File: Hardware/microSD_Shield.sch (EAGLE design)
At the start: 19 parts, among them J1 AVR_SPI_PRG_6NS, U1 USD-SOCKETNEW, U2 ARDUINO_R3_SHIELDNOLABELS, U3 HEX_CONVERTER

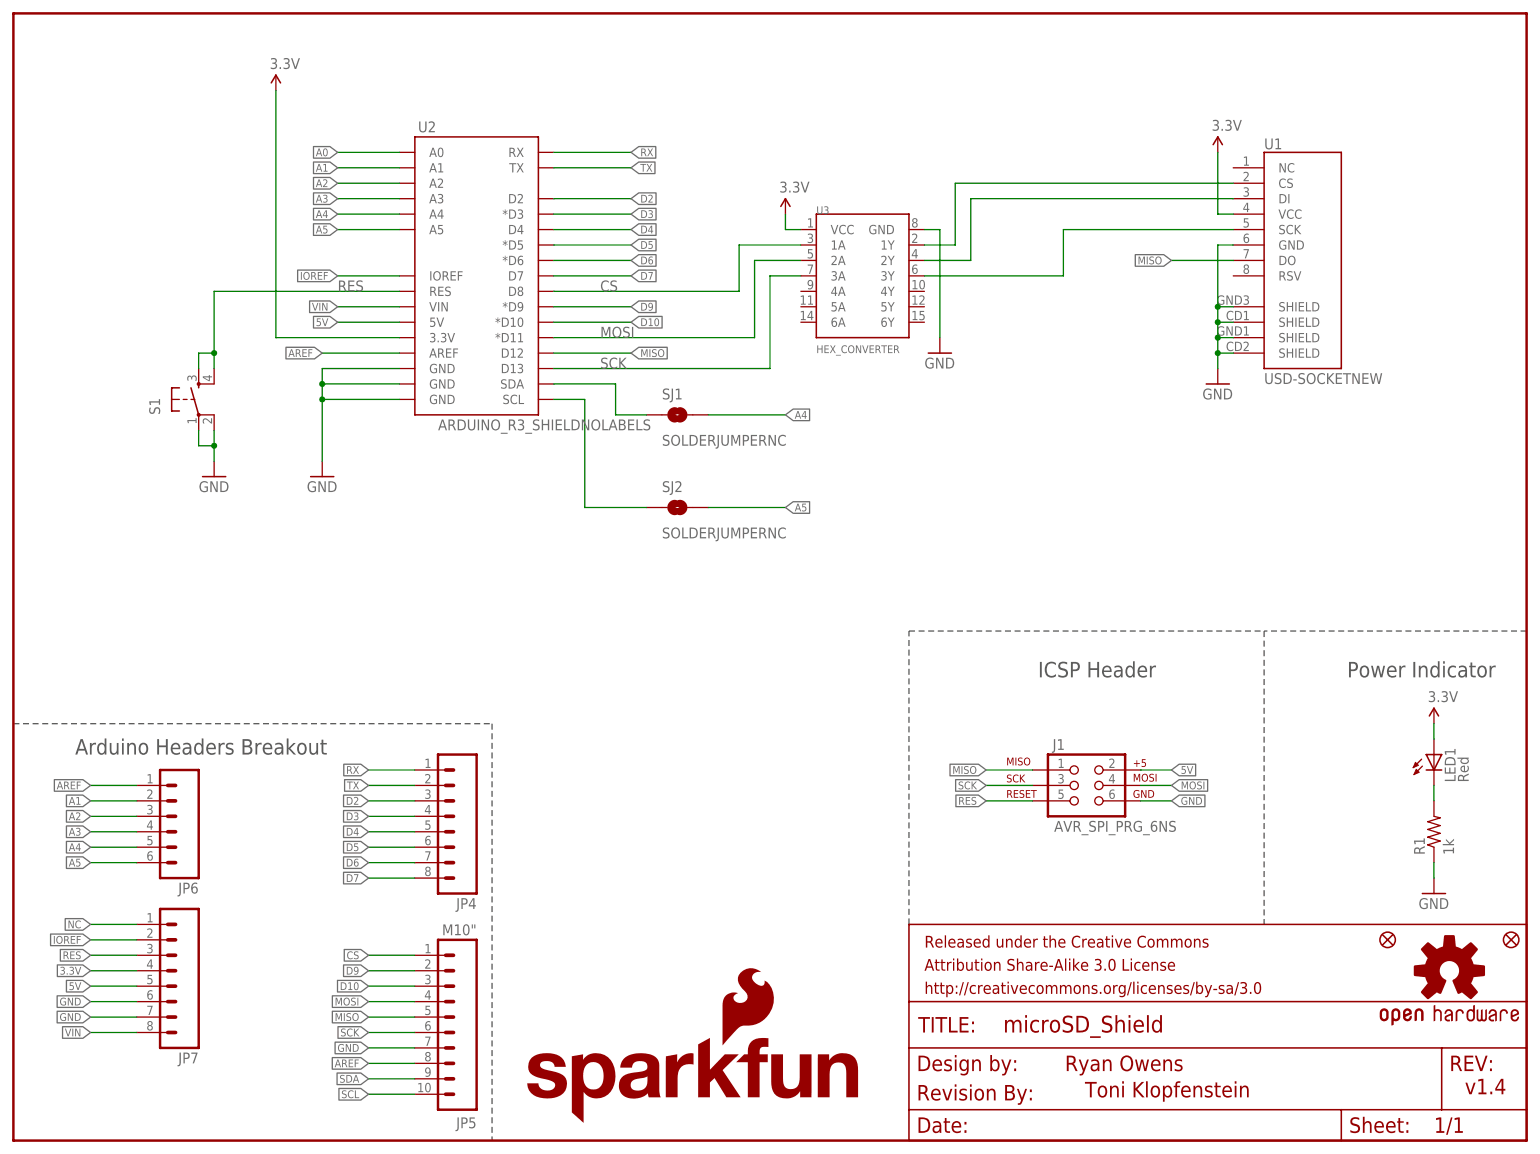
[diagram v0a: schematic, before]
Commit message: Adding decoupling capacitors
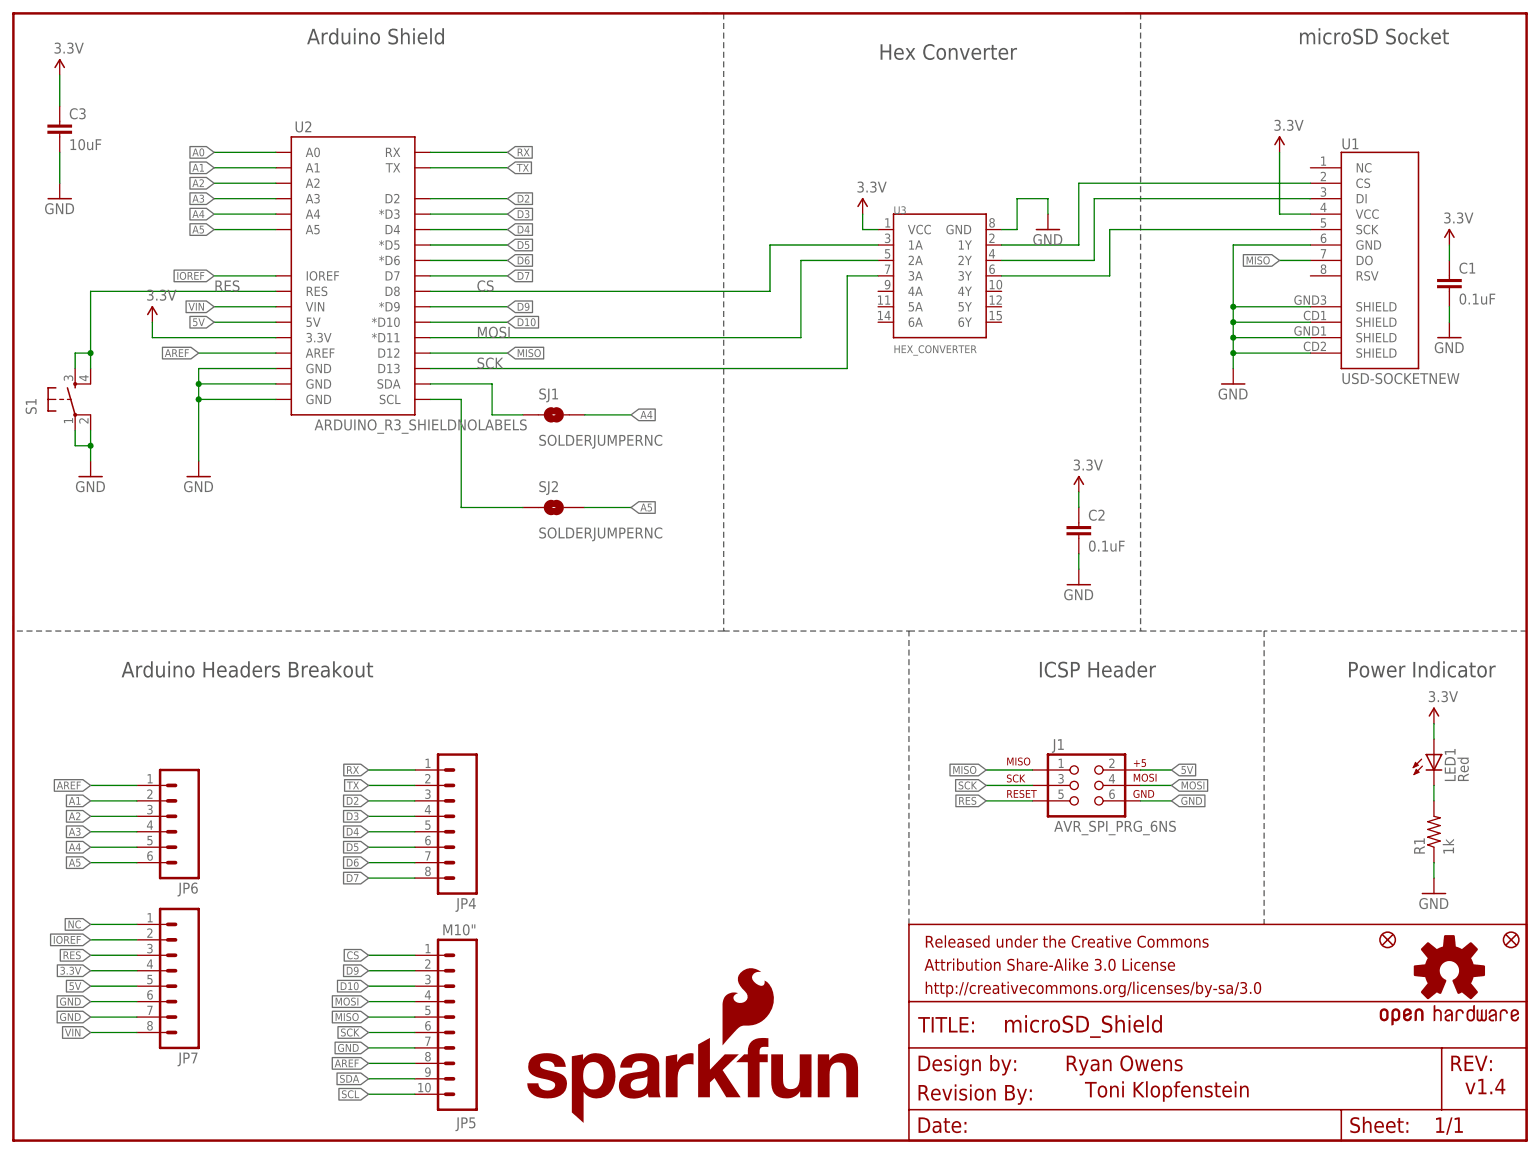
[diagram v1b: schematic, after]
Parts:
- added C1, C2: 0.1uF, SparkFun-Capacitors:0.1UF-25V-5%(0603)
- added C3: 10uF, SparkFun-Capacitors:10UF-6.3V-20%(0603)
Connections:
- net 3.3V: now also C1.1, C2.1, C3.1
- net GND: now also C1.2, C2.2, C3.2
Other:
- note added: "Arduino Shield"
- note added: "Hex Converter"
- note added: "microSD Socket"
- moved on the sheet: S1, SJ1, SJ2, U1, U2, U3

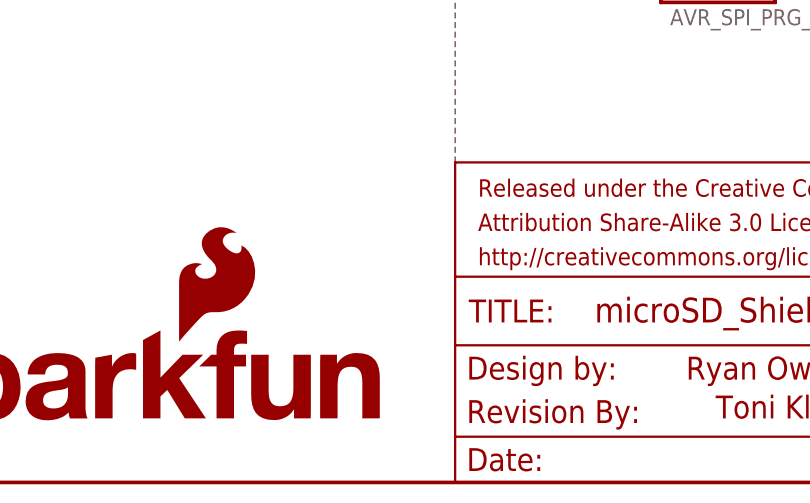
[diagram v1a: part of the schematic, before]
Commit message: Adding bottom flame to pcb
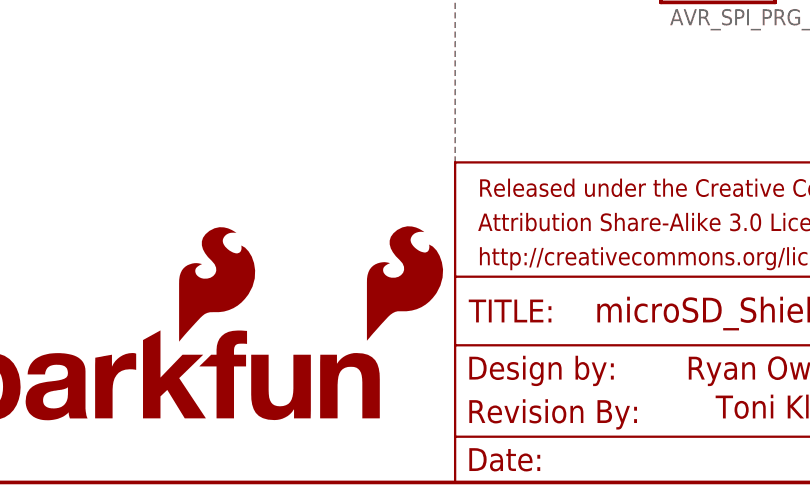
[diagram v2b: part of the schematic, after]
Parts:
- added LOGO2: SFE_LOGO_FLAME.1_INCH, SparkFun-Aesthetics:SFE_LOGO_FLAME.1_INCH
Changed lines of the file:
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@@
 <part name="P+6" library="SparkFun" deviceset="3.3V" device=""/>
 <part name="P+7" library="SparkFun" deviceset="3.3V" device=""/>
+<part name="LOGO2" library="SparkFun-Aesthetics" deviceset="SFE_LOGO_FLAME" device=".1_INCH"/>
 </parts>
 <sheets>
@@
 <instance part="P+6" gate="G$1" x="175.26" y="106.68"/>
 <instance part="P+7" gate="G$1" x="236.22" y="147.32"/>
+<instance part="LOGO2" gate="G$1" x="137.16" y="15.24"/>
 </instances>
 <busses>
